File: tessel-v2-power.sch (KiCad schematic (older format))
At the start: 51 parts, among them Q301 MMSS8550, U301 AAT4610, U302 AAT4610, U303 AP3417C, U304 AP3417C, U305 AP3418

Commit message: moving to intrernal RLC symbols...~half way there, by sheets
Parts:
- C301, C302, C303, C304, C305, C306, C307, C308, C309, C310, C311, C312, C313, C314, C315, C316, C317, C318, C319, C320, C321, C322, C323, C324, C325, C326, C327: symbol C -> TM_C
- L301, L302, L303: symbol INDUCTOR -> TM_L
- R301, R302, R303, R304, R305, R306, R307, R308, R309, R310, R311, R312, R313: symbol R -> TM_R
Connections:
- wire segments 137 -> 178
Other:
- note added: "SWAP: 453R"
- note removed: "Swap: 453R"

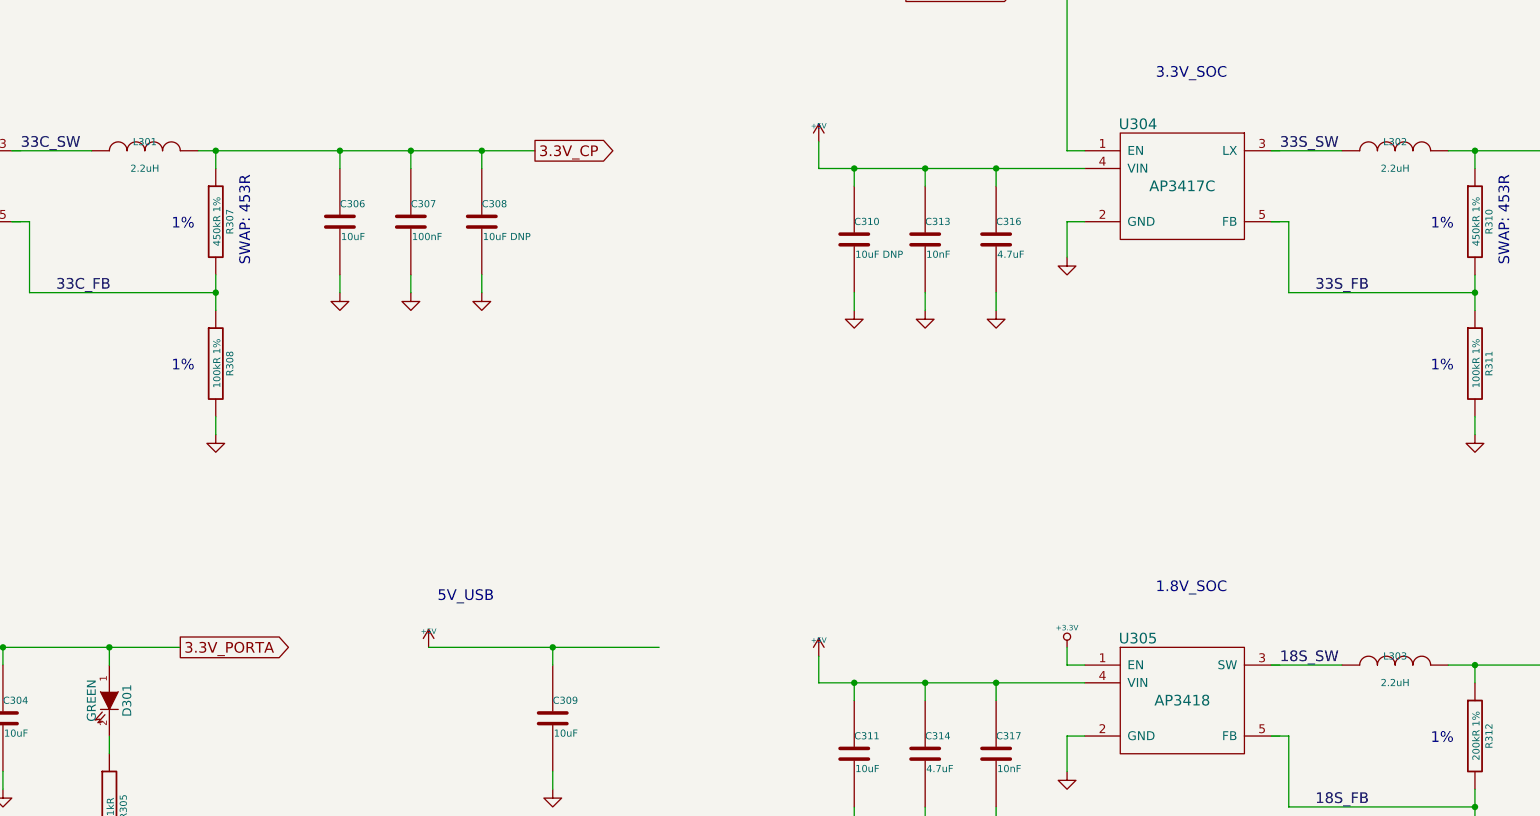
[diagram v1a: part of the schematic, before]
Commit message: swapped out all RLCs
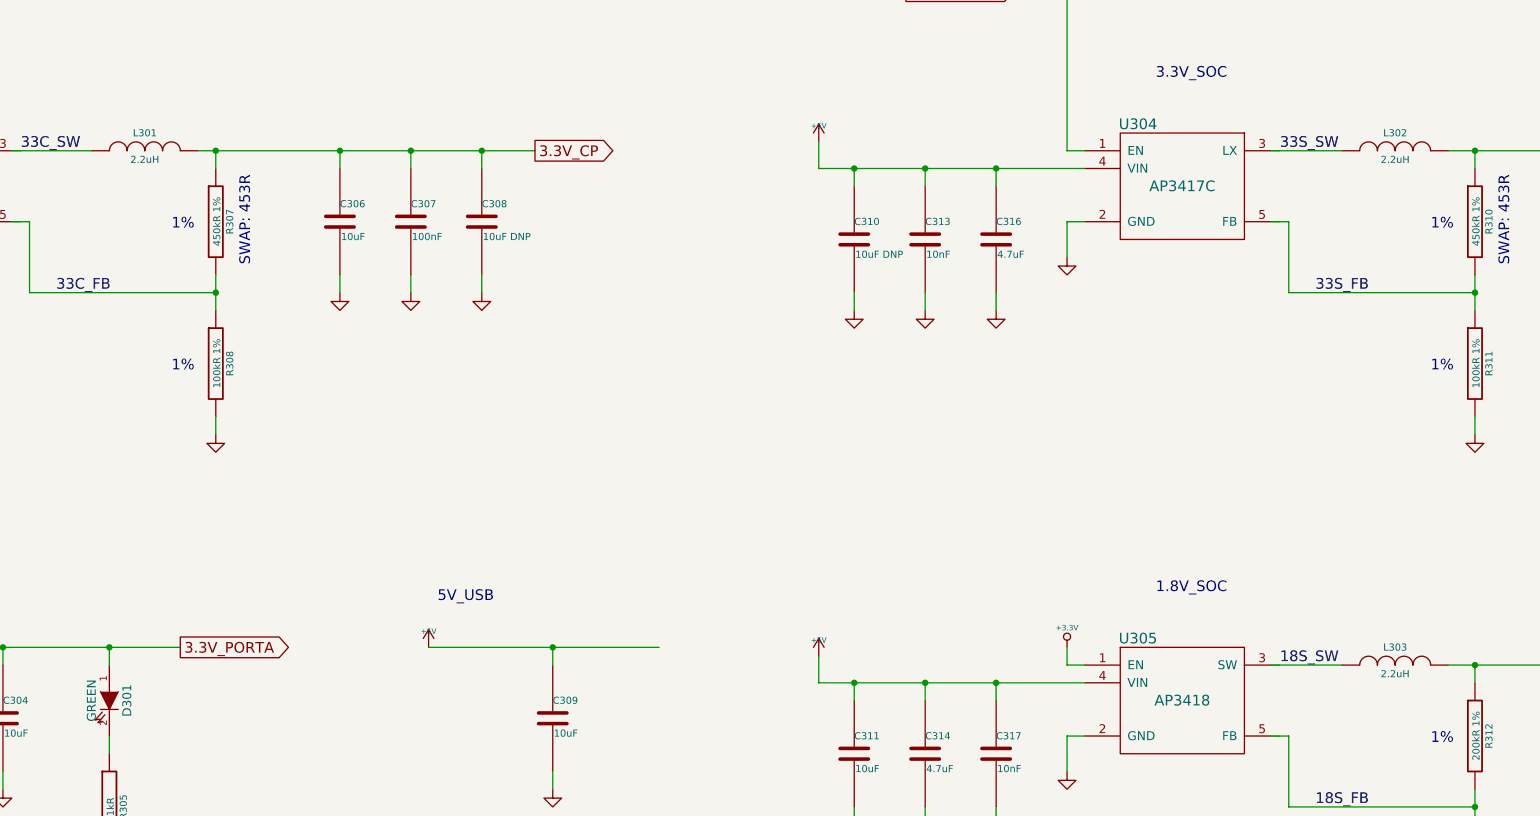
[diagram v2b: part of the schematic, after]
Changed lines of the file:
@@
 U 1 1 549071D8
 P 5200 2800
-F 0 "L301" V 5150 2800 40  0000 C CNN
-F 1 "2.2uH" V 5300 2800 40  0000 C CNN
+F 0 "L301" V 5100 2800 40  0000 C CNN
+F 1 "2.2uH" V 5250 2800 40  0000 C CNN
 F 2 "tm-kicad-lib:SWPA5020S" H 5200 2800 60  0001 C CNN
 F 3 "http://www.flight-elec.com/upload/suppliers/fe/20101239421550581.pdf" H 5200 2800 60  0001 C CNN
@@
 U 1 1 54BE0E0C
 P 12250 2800
-F 0 "L302" V 12200 2800 40  0000 C CNN
-F 1 "2.2uH" V 12350 2800 40  0000 C CNN
+F 0 "L302" V 12150 2800 40  0000 C CNN
+F 1 "2.2uH" V 12300 2800 40  0000 C CNN
 F 2 "tm-kicad-lib:SWPA5020S" H 12250 2800 60  0001 C CNN
 F 3 "http://www.flight-elec.com/upload/suppliers/fe/20101239421550581.pdf" H 12250 2800 60  0001 C CNN
@@
 U 1 1 54BE3760
 P 12250 5700
-F 0 "L303" V 12200 5700 40  0000 C CNN
-F 1 "2.2uH" V 12350 5700 40  0000 C CNN
+F 0 "L303" V 12150 5700 40  0000 C CNN
+F 1 "2.2uH" V 12300 5700 40  0000 C CNN
 F 2 "tm-kicad-lib:SWPA5020S" H 12250 5700 60  0001 C CNN
 F 3 "http://www.flight-elec.com/upload/suppliers/fe/20101239421550581.pdf" H 12250 5700 60  0001 C CNN

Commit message: project save
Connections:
- wire segments 178 -> 137

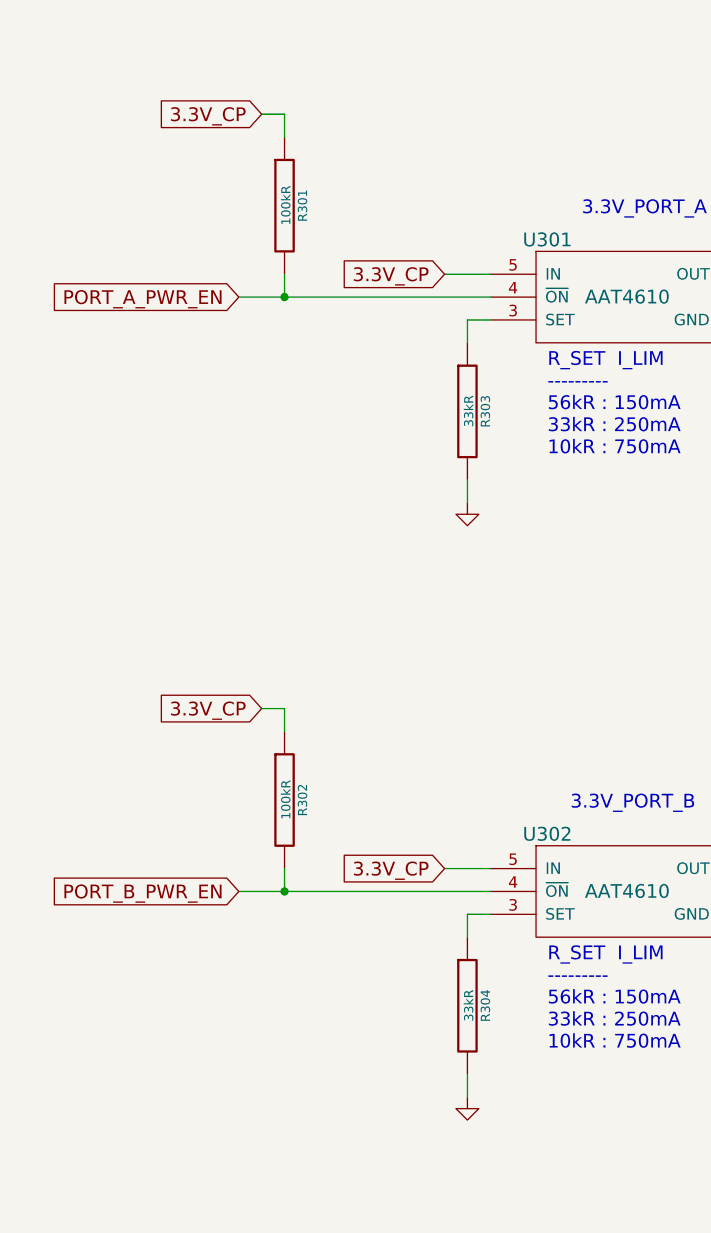
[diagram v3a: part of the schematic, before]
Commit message: swapped pull resistor direction for module port power enable, kept footprint as dnp
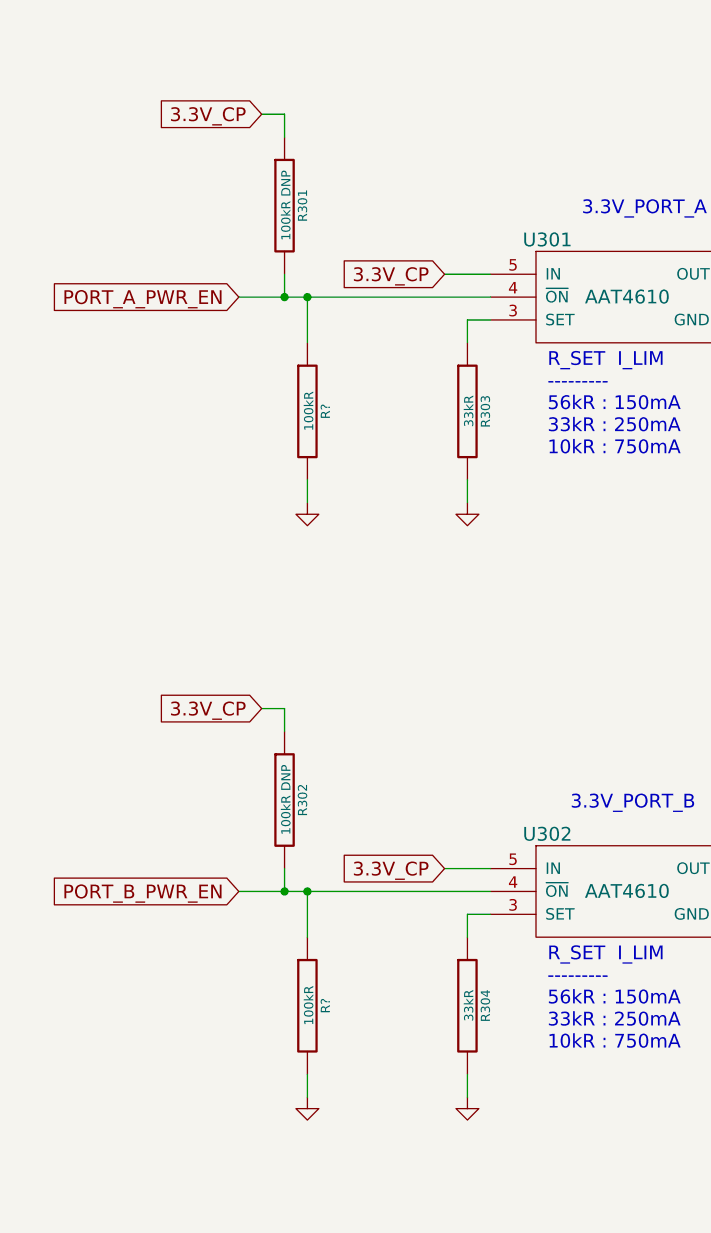
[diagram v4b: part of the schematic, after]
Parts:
- added R? (x2): 100kR, tm-kicad-lib:SMD-0402-R, symbol TM_R
- R301, R302: value 100kR -> 100kR DNP
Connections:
- wire segments 137 -> 141
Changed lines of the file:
@@
 P 1900 5300
 F 0 "R301" V 1980 5300 40  0000 C CNN
-F 1 "100kR" V 1907 5301 40  0000 C CNN
+F 1 "100kR DNP" V 1907 5301 40  0000 C CNN
 F 2 "tm-kicad-lib:SMD-0402-R" V 1830 5300 30  0001 C CNN
 F 3 "" H 1900 5300 30  0000 C CNN
@@
 P 1900 7900
 F 0 "R302" V 1980 7900 40  0000 C CNN
-F 1 "100kR" V 1907 7901 40  0000 C CNN
+F 1 "100kR DNP" V 1907 7901 40  0000 C CNN
 F 2 "tm-kicad-lib:SMD-0402-R" V 1830 7900 30  0001 C CNN
 F 3 "" H 1900 7900 30  0000 C CNN
@@
 	5000 8200 5000 8300
 Connection ~ 5000 8200
+$Comp
+L TM_R R?
+U 1 1 55071E19
+P 2000 6200
+F 0 "R?" V 2080 6200 40  0000 C CNN
+F 1 "100kR" V 2007 6201 40  0000 C CNN
+F 2 "tm-kicad-lib:SMD-0402-R" V 1930 6200 30  0001 C CNN
+F 3 "" H 2000 6200 30  0000 C CNN
+	1    2000 6200
+	1    0    0    -1
+$EndComp
+Wire Wire Line
+	2000 5900 2000 5700
+Connection ~ 2000 5700
+$Comp
+L GND #PWR?
+U 1 1 55072009
+P 2000 6600
+F 0 "#PWR?" H 2000 6600 30  0001 C CNN
+F 1 "GND" H 2000 6530 30  0001 C CNN
+F 2 "" H 2000 6600 60  0000 C CNN
+F 3 "" H 2000 6600 60  0000 C CNN
+	1    2000 6600
+	1    0    0    -1
+$EndComp
+Wire Wire Line
+	2000 6500 2000 6600
+$Comp
+L TM_R R?
+U 1 1 55072090
+P 2000 8800
+F 0 "R?" V 2080 8800 40  0000 C CNN
+F 1 "100kR" V 2007 8801 40  0000 C CNN
+F 2 "tm-kicad-lib:SMD-0402-R" V 1930 8800 30  0001 C CNN
+F 3 "" H 2000 8800 30  0000 C CNN
+	1    2000 8800
+	1    0    0    -1
+$EndComp
+Wire Wire Line
+	2000 8500 2000 8300
+$Comp
+L GND #PWR?
+U 1 1 55072097
+P 2000 9200
+F 0 "#PWR?" H 2000 9200 30  0001 C CNN
+F 1 "GND" H 2000 9130 30  0001 C CNN
+F 2 "" H 2000 9200 60  0000 C CNN
+F 3 "" H 2000 9200 60  0000 C CNN
+	1    2000 9200
+	1    0    0    -1
+$EndComp
+Wire Wire Line
+	2000 9100 2000 9200
+Connection ~ 2000 8300
 $EndSCHEMATC

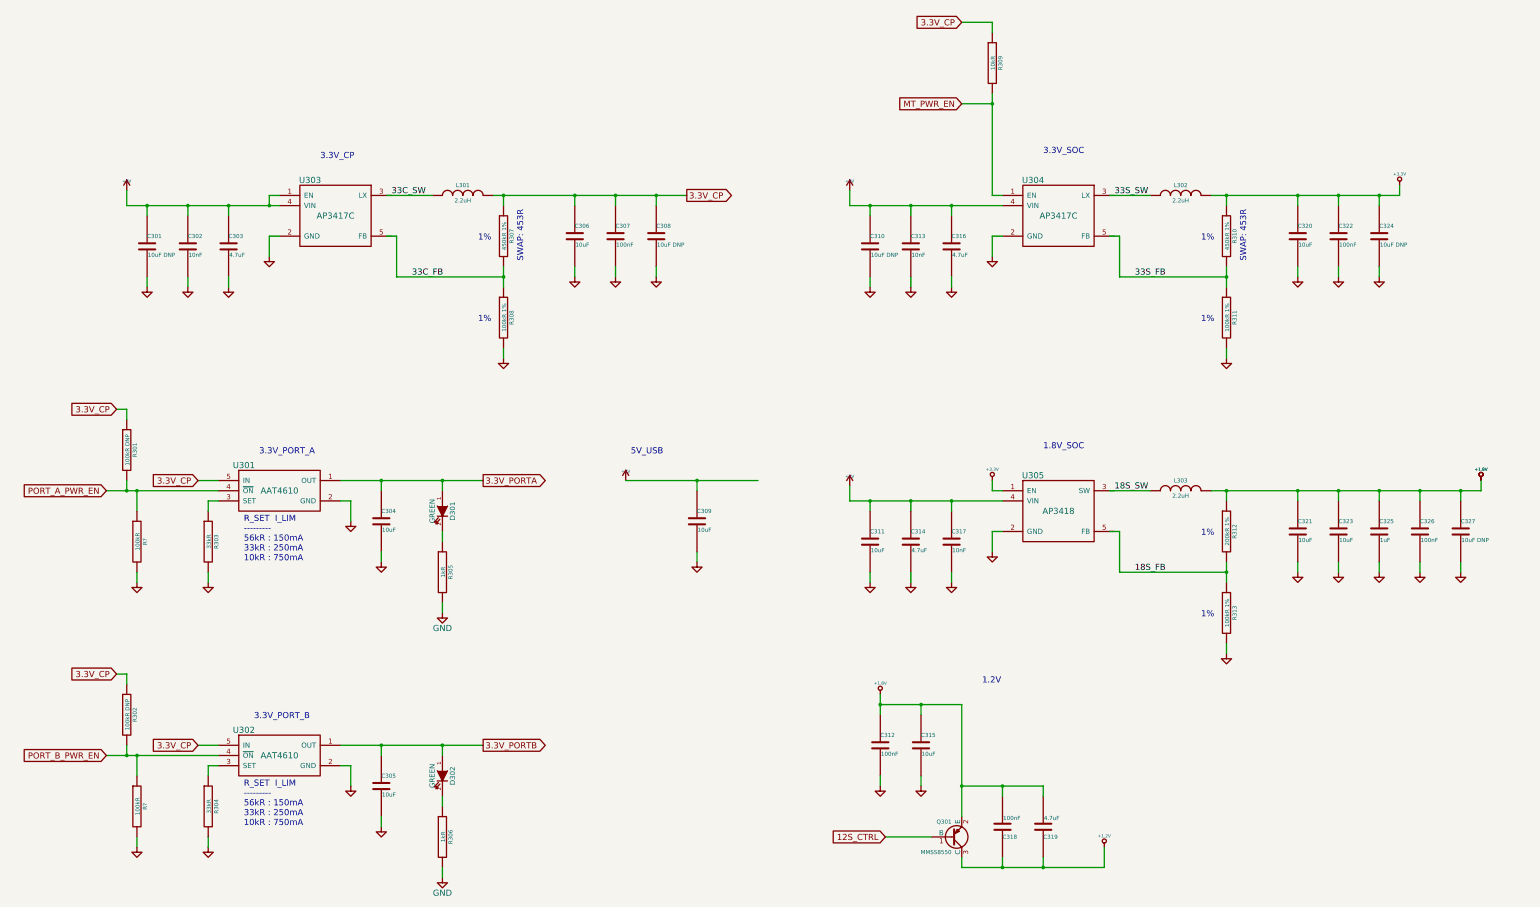
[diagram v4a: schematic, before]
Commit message: added 5v headers
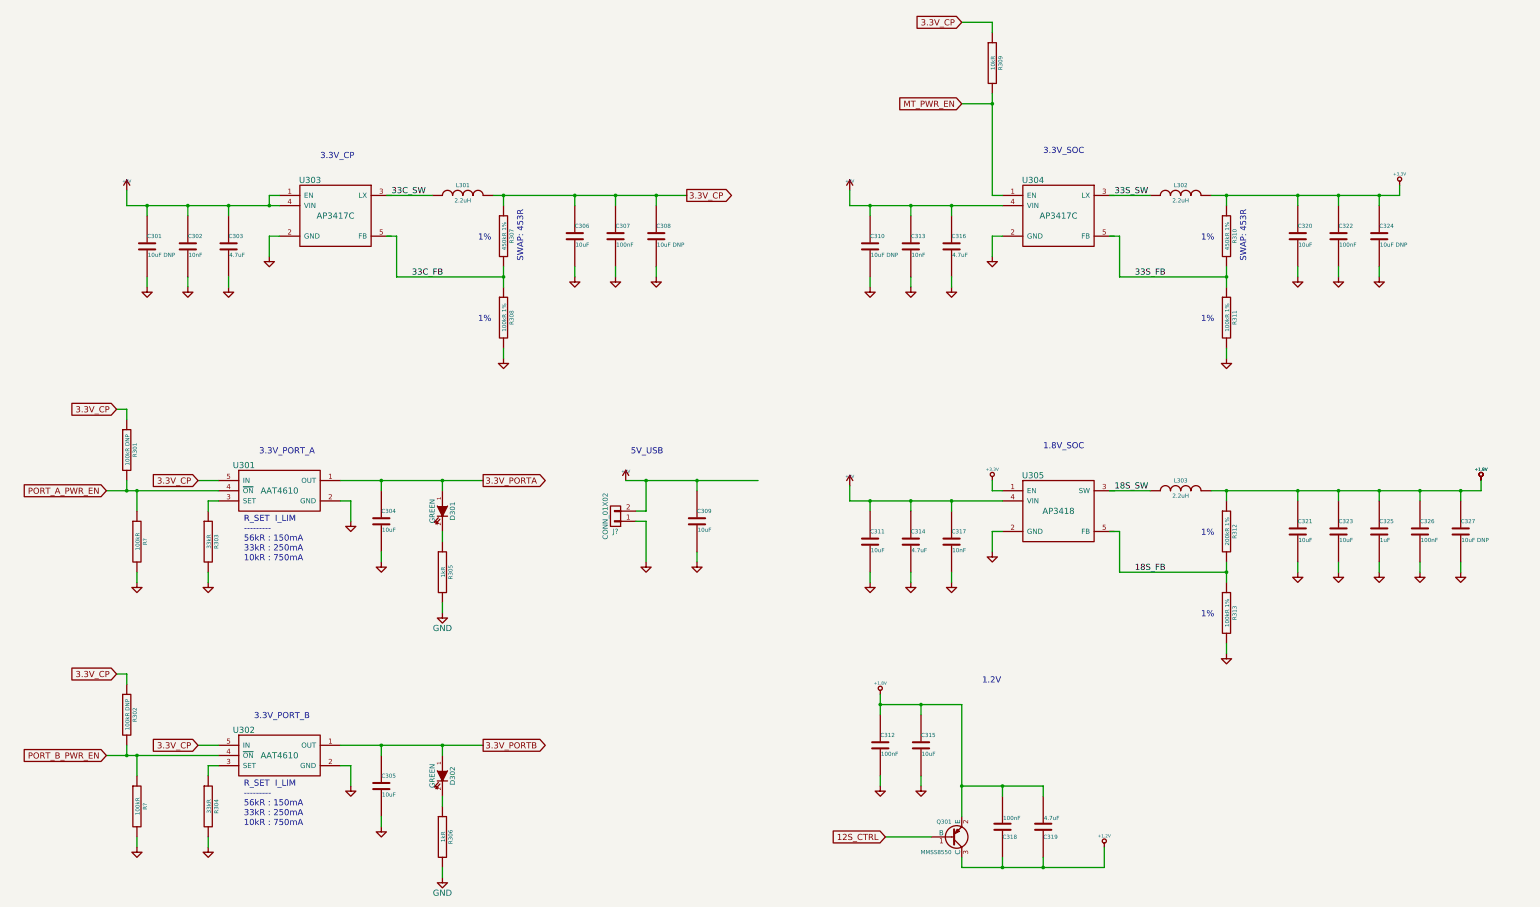
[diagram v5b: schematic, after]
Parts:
- added J?: CONN_01X02, symbol CONN_01X02
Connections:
- wire segments 141 -> 189
